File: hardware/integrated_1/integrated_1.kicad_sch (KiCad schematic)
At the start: 8 parts, among them J1 USB4105-GF-A-120, J2 HDMI_A_1.4, J3 Debug Header

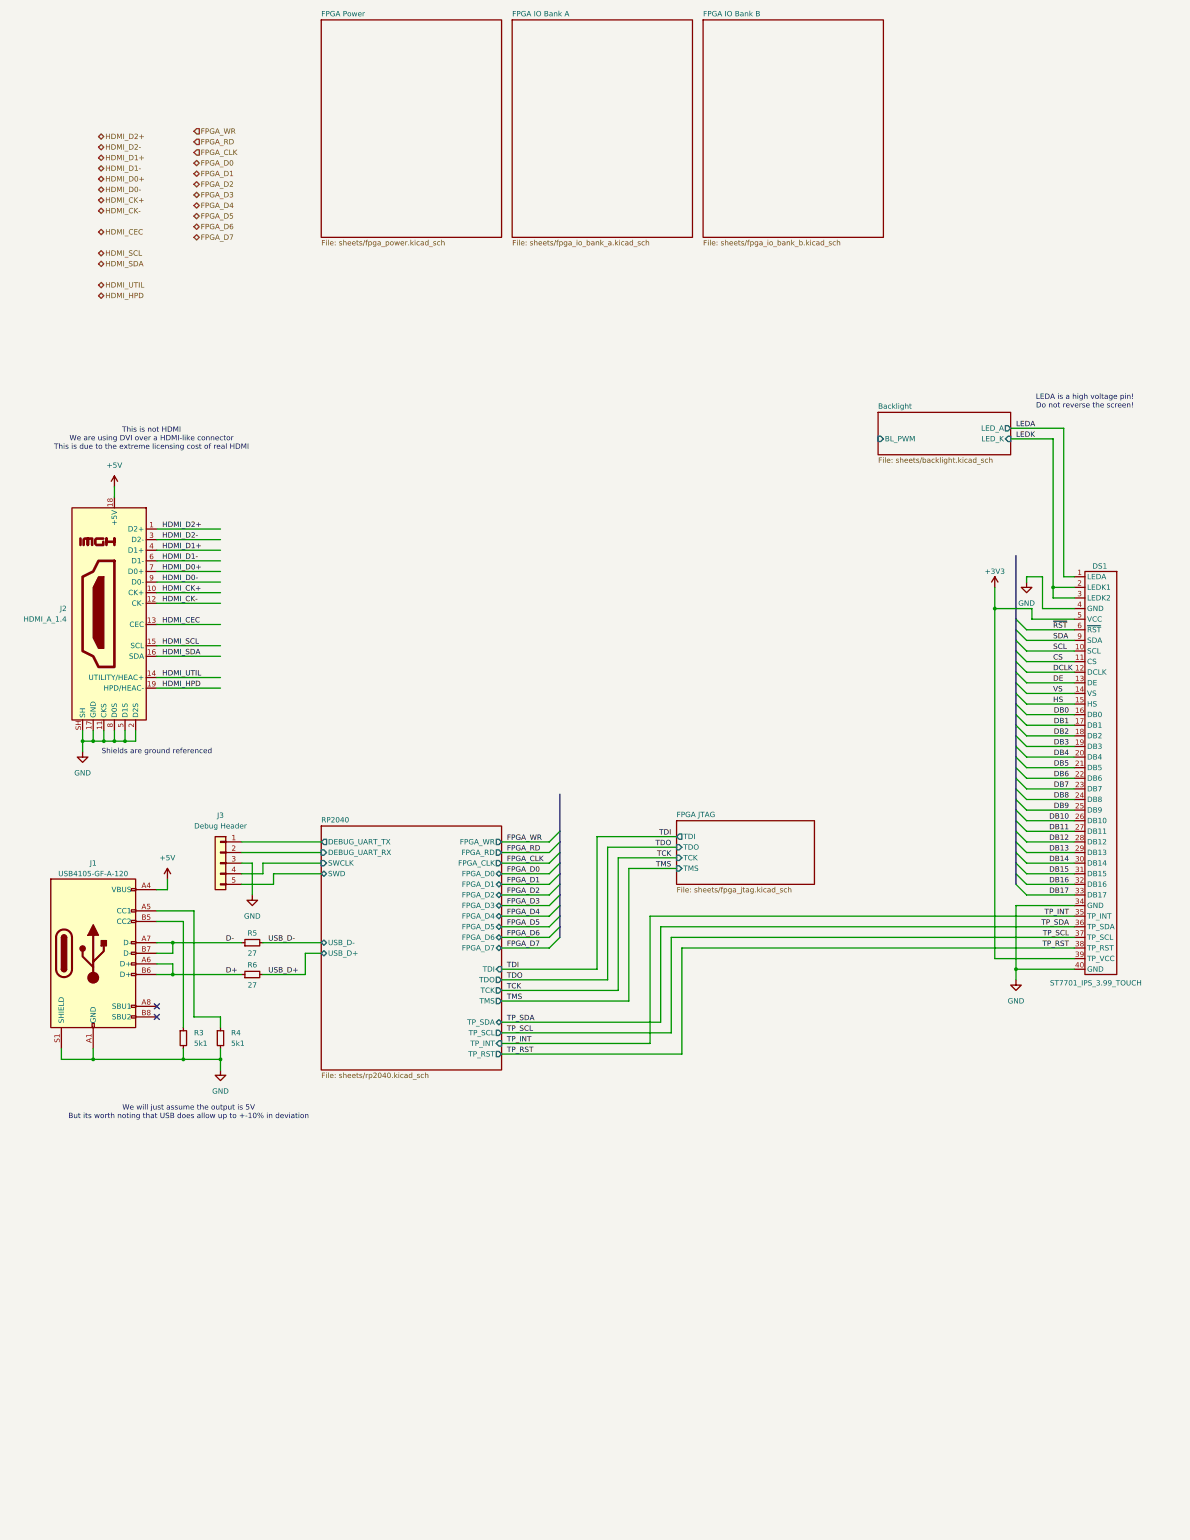
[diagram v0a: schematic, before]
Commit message: renaming a few pins
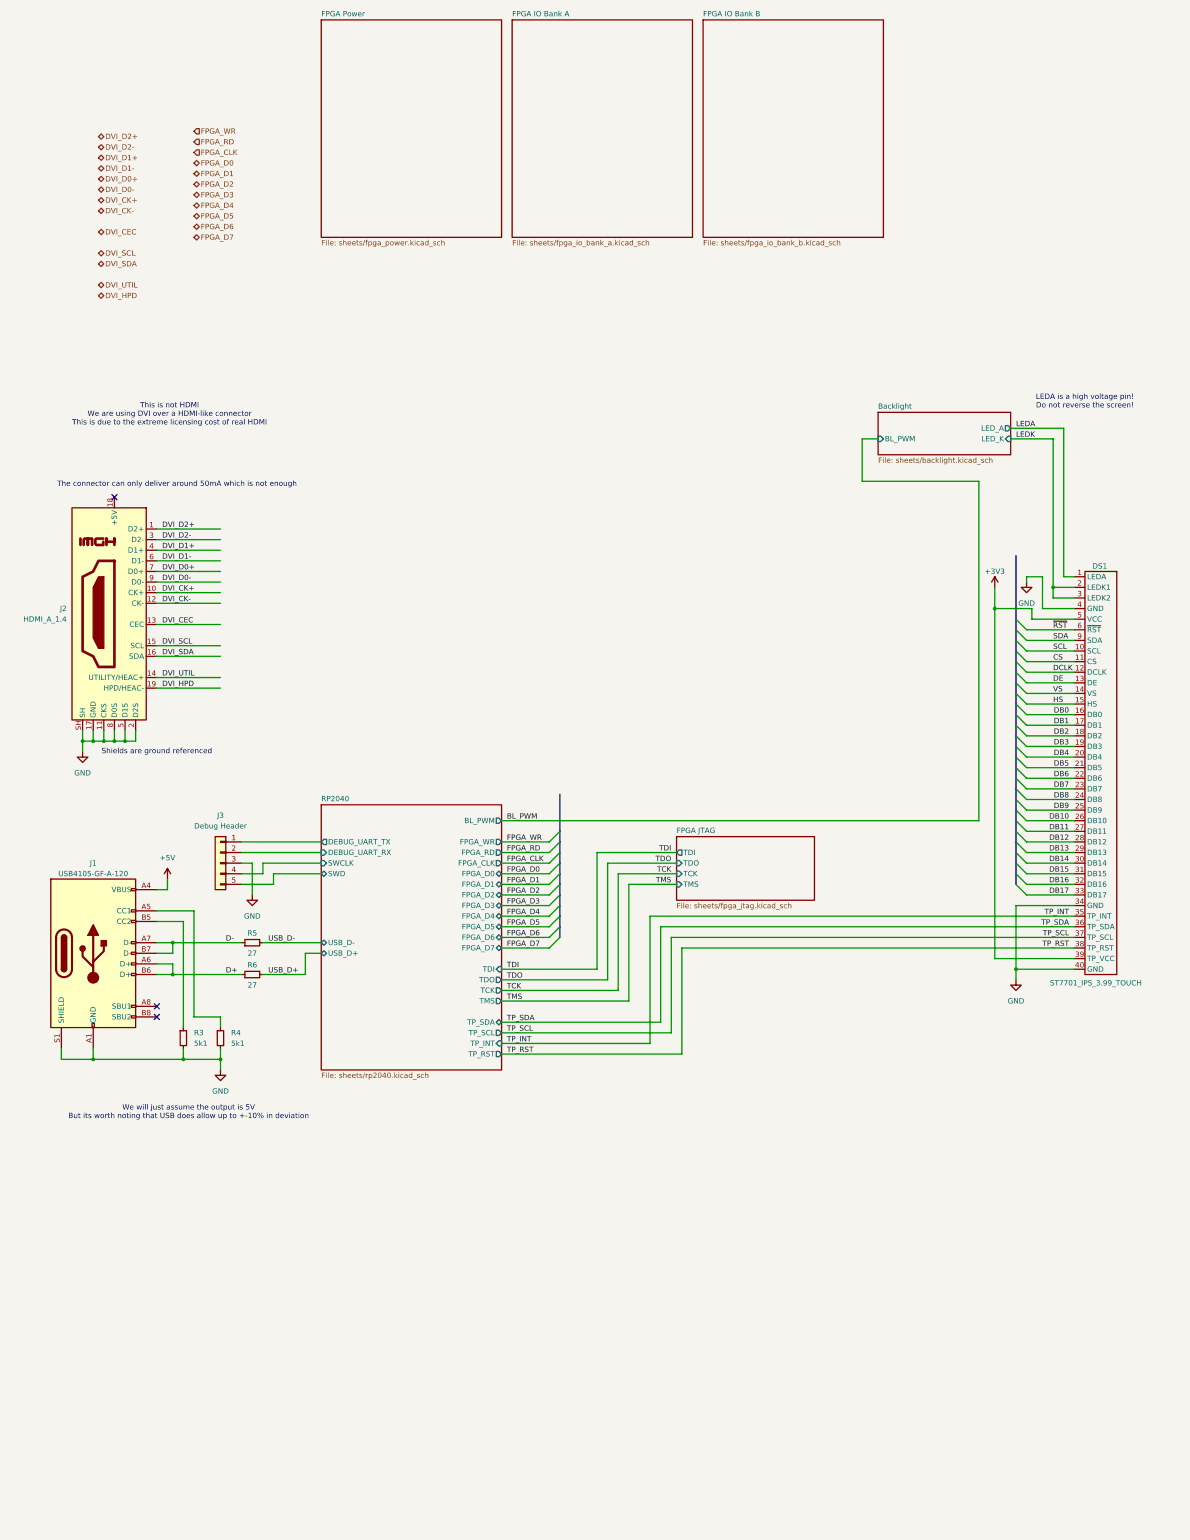
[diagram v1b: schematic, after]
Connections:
- net +5V: no longer J2.18 (+5V)
- net HDMI_CEC renamed DVI_CEC
- net HDMI_CK+ renamed DVI_CK+
- net HDMI_CK- renamed DVI_CK-
- net HDMI_D0+ renamed DVI_D0+
- net HDMI_D0- renamed DVI_D0-
- net HDMI_D1+ renamed DVI_D1+
- net HDMI_D1- renamed DVI_D1-
- net HDMI_D2+ renamed DVI_D2+
- net HDMI_D2- renamed DVI_D2-
- net HDMI_HPD renamed DVI_HPD
- net HDMI_SCL renamed DVI_SCL
- net HDMI_SDA renamed DVI_SDA
- net HDMI_UTIL renamed DVI_UTIL
- no-connect marks 2 -> 3
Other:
- sheet RP2040 ports: added BL_PWM; removed none
- note added: "The connector can only deliver around 50mA which is not enough"

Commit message: added top level connections between the fpga modules
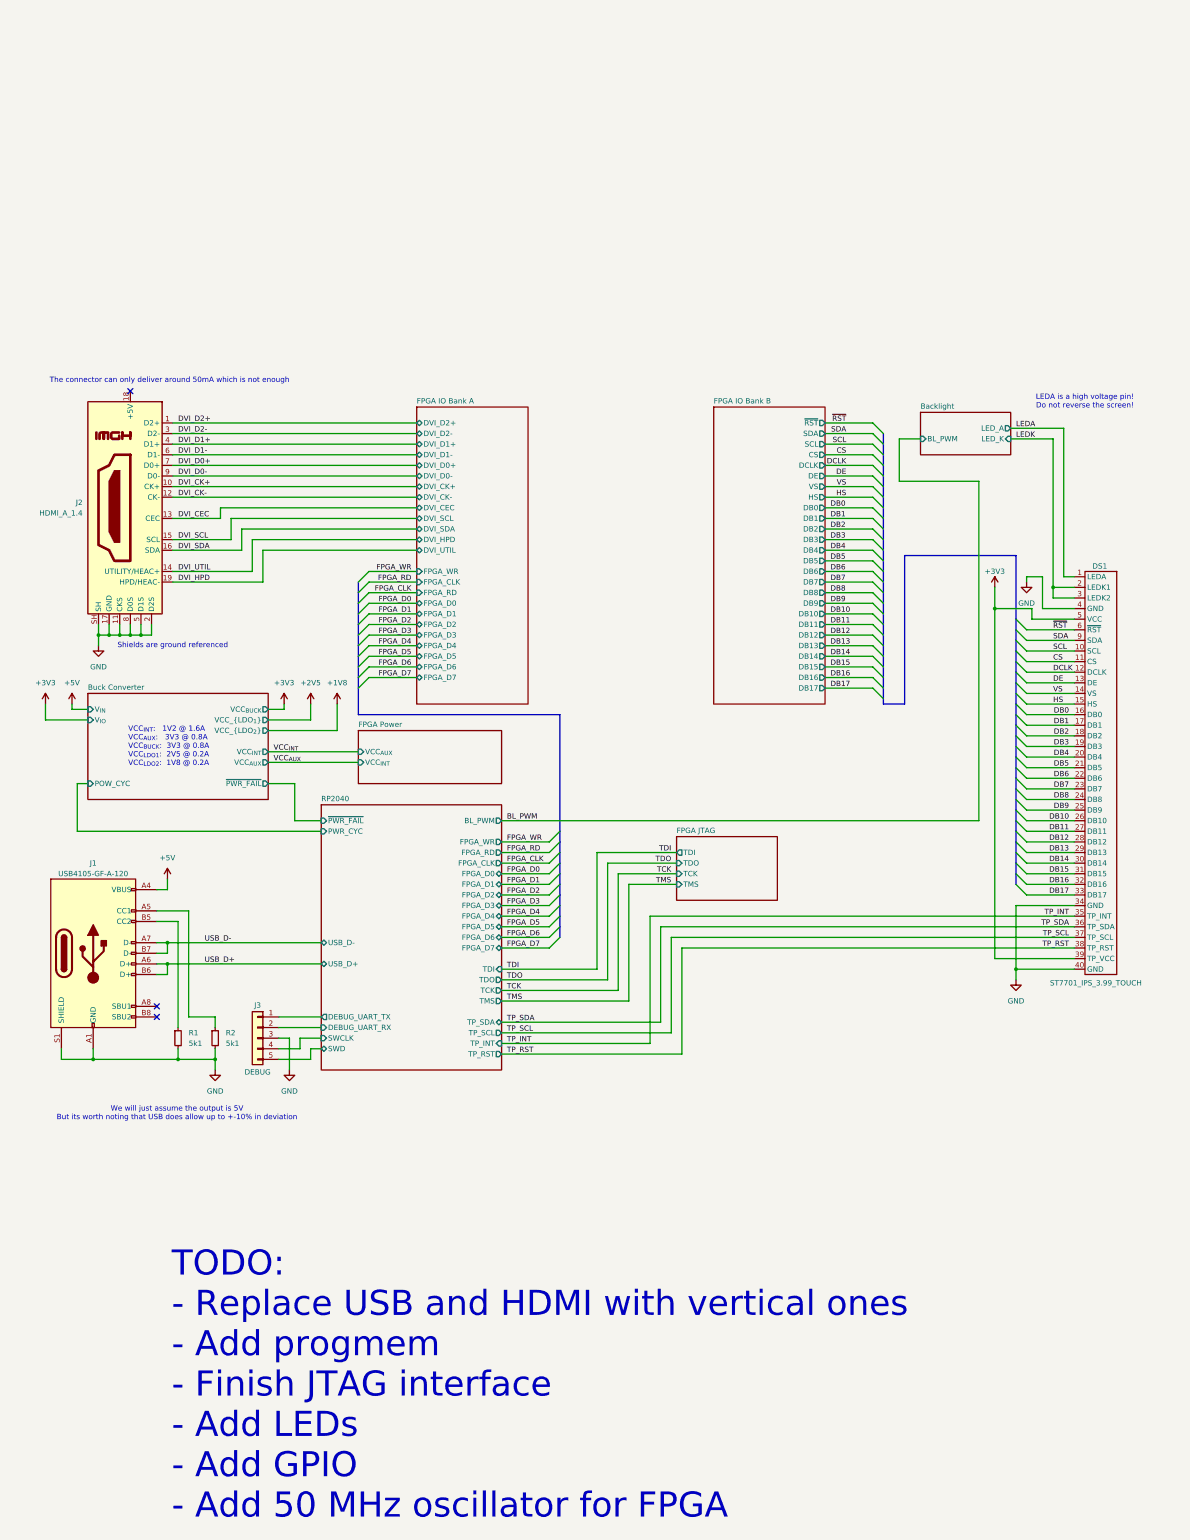
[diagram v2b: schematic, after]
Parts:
- removed R5, R6: 27, Resistor_SMD:R_0603_1608Metric, symbol Device:R_Small
- J2: footprint (none) -> Connector_HDMI:HDMI_A_Molex_208658-1001_Horizontal
- J3: value Debug Header -> DEBUG
- R1: renamed from R3; footprint Resistor_SMD:R_0603_1608Metric -> Resistor_SMD:R_0402_1005Metric
- R2: renamed from R4; footprint Resistor_SMD:R_0603_1608Metric -> Resistor_SMD:R_0402_1005Metric
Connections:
- net D+ is gone; now on net USB_D+: J1.A6 (D+), J1.B6 (D+)
- net D- is gone; now on net USB_D-: J1.A7 (D-), J1.B7 (D-)
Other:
- added sheet Buck Converter (sheets/buck_power.kicad_sch)
- sheet FPGA IO Bank A ports: added DVI_CEC, DVI_CK+, DVI_CK-, DVI_D0+, DVI_D0-, DVI_D1+, DVI_D1-, DVI_D2+, DVI_D2-, DVI_HPD, DVI_SCL, DVI_SDA, DVI_UTIL, FPGA_CLK, FPGA_D0, FPGA_D1, FPGA_D2, FPGA_D3, FPGA_D4, FPGA_D5, FPGA_D6, FPGA_D7, FPGA_RD, FPGA_WR; removed none
- sheet FPGA IO Bank B ports: added CS, DB0, DB1, DB10, DB11, DB12, DB13, DB14, DB15, DB16, DB17, DB2, DB3, DB4, DB5, DB6, DB7, DB8, DB9, DCLK, DE, HS, SCL, SDA, VS, ~{RST}; removed none
- sheet FPGA Power ports: added VCC_{AUX}, VCC_{INT}; removed none
- sheet RP2040 ports: added PWR_CYC, ~{PWR_FAIL}; removed none
- note added: "TODO: - Replace USB and HDMI with vertical ones - Add progmem - Finish JTAG interface - Add LEDs - Add GPIO - Add 50 MHz oscillator for FPGA"
- note added: "VCC_{INT}: 1V2 @ 1.6A VCC_{AUX}: 3V3 @ 0.8A VCC_{BUCK}: 3V3 @ 0.8A VCC_{LDO1}: 2V5 @ 0.2A VCC_{LDO2}: 1V8 @ 0.2A"
- note removed: "This is not HDMI We are using DVI over a HDMI-like connector This is due to the extreme licensing cost of real HDMI"
- moved on the sheet: J2, J3, R1, R2

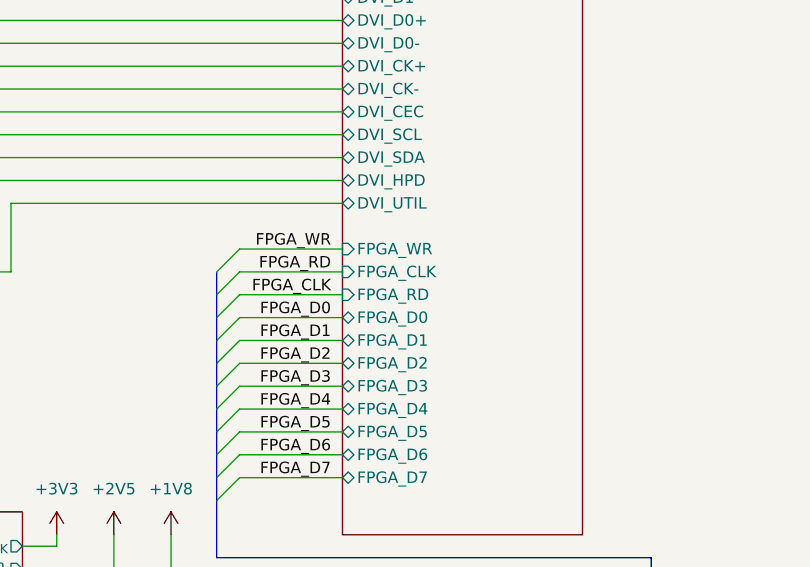
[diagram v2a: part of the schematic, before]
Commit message: rearranged the pinout to make more sense
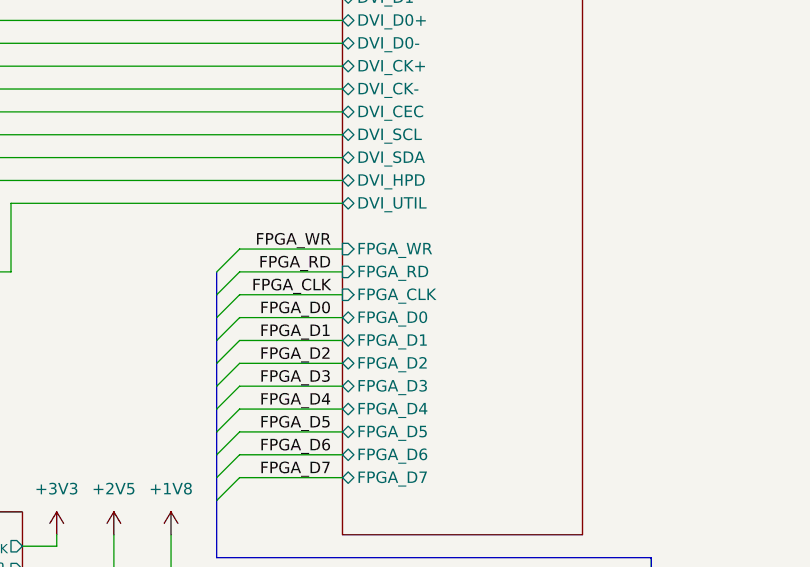
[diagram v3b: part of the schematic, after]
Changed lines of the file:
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@@
 		)
 		(pin "FPGA_RD" input
-			(at 105.41 66.04 180)
+			(at 105.41 63.5 180)
 			(effects
 				(font
@@
 		)
 		(pin "FPGA_CLK" input
-			(at 105.41 63.5 180)
+			(at 105.41 66.04 180)
 			(effects
 				(font
